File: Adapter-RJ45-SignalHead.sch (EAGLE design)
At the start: 4 parts, among them CON1 CONNECTOR-GROVE-4P-2.0-347013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, CON2 CONNECTOR-GROVE-4P-2.0-347013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

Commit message: V3.2 - added CUT-R
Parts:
- added CON3, CON4: (no value), SPCoast:CONNECTOR-M04LOCK
- added R1, R2, R3, R4, R5, R6: (no value), SPCoast:RPTH-R0
- CON1, CON2: value CONNECTOR-GROVE-4P-2.0-3470130P1 -> (none)
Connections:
- removed net L5: CON2.1, J1.5
- removed net L6: CON2.2, J1.6
- removed net L7: CON2.3, J1.7
- removed net L8: CON2.4, J1.8
- removed net N$1: CON1.1, J1.1
- removed net N$2: CON1.2, J1.2
- removed net N$3: CON1.3, J1.3
- removed net N$4: CON1.4, J1.4
- new net A-COMMON: CON1.4, CON4.4, J1.4
- new net AG: J1.1, R6.2
- new net AGR: CON1.1, CON4.1, R6.1
- new net AR: J1.3, R4.2
- new net ARR: CON1.3, CON4.3, R4.1
- new net AY: J1.2, R5.2
- new net AYR: CON1.2, CON4.2, R5.1
- new net B-COMMON: CON2.4, CON3.4, J1.8
- new net BG: J1.5, R3.2
- new net BGR: CON2.1, CON3.1, R3.1
- new net BR: J1.7, R1.2
- new net BRR: CON2.3, CON3.3, R1.1
- new net BY: J1.6, R2.2
- new net BYR: CON2.2, CON3.2, R2.1
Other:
- note added: "2x 2mm 4-pin"
- note added: "Signal Head Breakout"
- note added: "v3.2"
- note added: "w/ optional resistors"
- note removed: "CMRI Breakout"
- note removed: "RJ45 adapter"
- note removed: "v3.1"
- moved on the sheet: CON1, CON2, J1

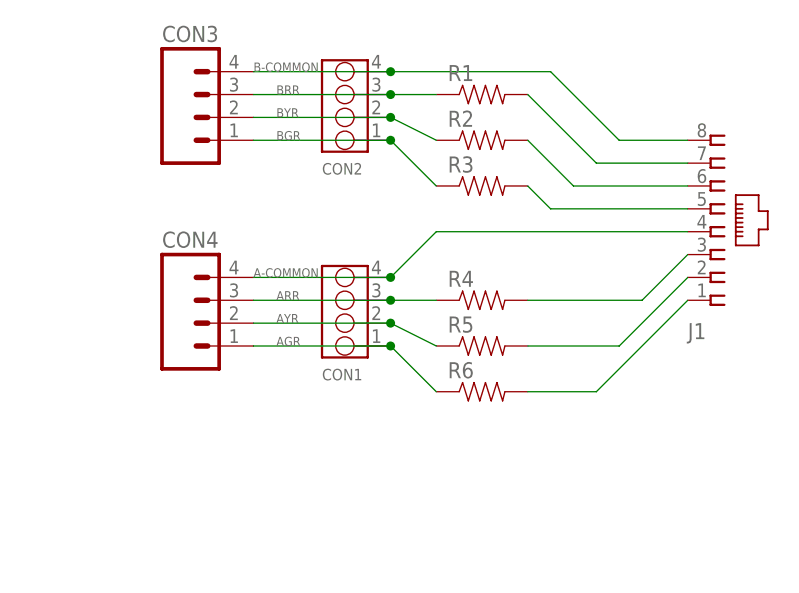
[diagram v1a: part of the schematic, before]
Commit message: added values for connectors
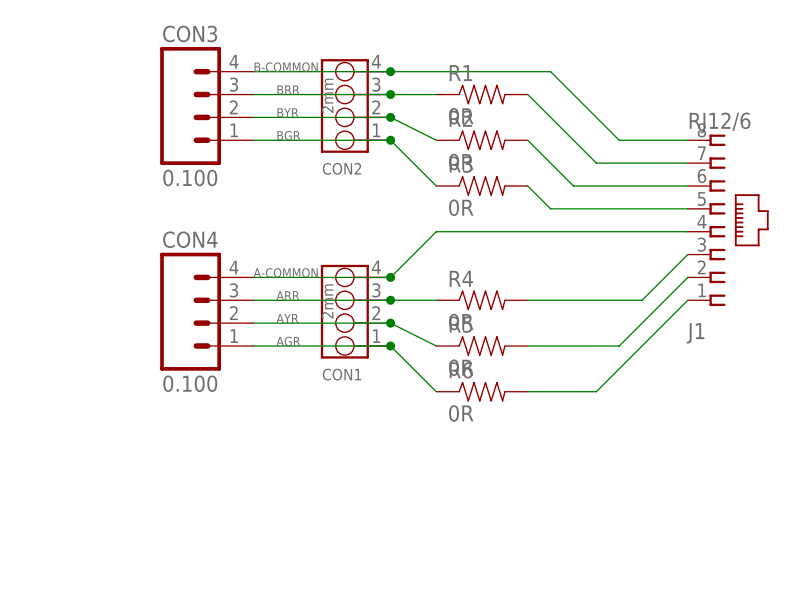
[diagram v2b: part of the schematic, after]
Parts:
- CON1, CON2: value (none) -> 2mm
- CON3, CON4: value (none) -> 0.100
- J1: value (none) -> RJ12/6
- R1, R2, R3, R4, R5, R6: value (none) -> 0R
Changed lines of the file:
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@@
 <grid distance="100" unitdist="mil" unit="mil" style="dots" multiple="1" display="yes" altdistance="50" altunitdist="mil" altunit="mil"/>
 <layers>
-<layer number="1" name="Top" color="4" fill="1" visible="yes" active="no"/>
-<layer number="2" name="Route2" color="1" fill="3" visible="yes" active="no"/>
-<layer number="3" name="Route3" color="4" fill="3" visible="yes" active="no"/>
-<layer number="14" name="Route14" color="1" fill="6" visible="yes" active="no"/>
-<layer number="15" name="Route15" color="4" fill="6" visible="yes" active="no"/>
-<layer number="16" name="Bottom" color="2" fill="1" visible="yes" active="no"/>
-<layer number="17" name="Pads" color="23" fill="1" visible="yes" active="no"/>
-<layer number="18" name="Vias" color="29" fill="1" visible="yes" active="no"/>
-<layer number="19" name="Unrouted" color="6" fill="1" visible="yes" active="no"/>
-<layer number="20" name="Dimension" color="15" fill="1" visible="yes" active="no"/>
-<layer number="21" name="tPlace" color="19" fill="1" visible="yes" active="no"/>
-<layer number="22" name="bPlace" color="17" fill="1" visible="yes" active="no"/>
-<layer number="23" name="tOrigins" color="30" fill="1" visible="yes" active="no"/>
-<layer number="24" name="bOrigins" color="15" fill="1" visible="yes" active="no"/>
-<layer number="25" name="tNames" color="63" fill="1" visible="yes" active="no"/>
-<layer number="26" name="bNames" color="34" fill="1" visible="yes" active="no"/>
-<layer number="27" name="tValues" color="56" fill="1" visible="yes" active="no"/>
-<layer number="28" name="bValues" color="7" fill="1" visible="yes" active="no"/>
+<layer number="1" name="Top" color="4" fill="1" visible="no" active="no"/>
+<layer number="2" name="Route2" color="1" fill="3" visible="no" active="no"/>
+<layer number="3" name="Route3" color="4" fill="3" visible="no" active="no"/>
+<layer number="14" name="Route14" color="1" fill="6" visible="no" active="no"/>
+<layer number="15" name="Route15" color="4" fill="6" visible="no" active="no"/>
+<layer number="16" name="Bottom" color="2" fill="1" visible="no" active="no"/>
+<layer number="17" name="Pads" color="23" fill="1" visible="no" active="no"/>
+<layer number="18" name="Vias" color="29" fill="1" visible="no" active="no"/>
+<layer number="19" name="Unrouted" color="6" fill="1" visible="no" active="no"/>
+<layer number="20" name="Dimension" color="15" fill="1" visible="no" active="no"/>
+<layer number="21" name="tPlace" color="19" fill="1" visible="no" active="no"/>
+<layer number="22" name="bPlace" color="17" fill="1" visible="no" active="no"/>
+<layer number="23" name="tOrigins" color="30" fill="1" visible="no" active="no"/>
+<layer number="24" name="bOrigins" color="15" fill="1" visible="no" active="no"/>
+<layer number="25" name="tNames" color="63" fill="1" visible="no" active="no"/>
+<layer number="26" name="bNames" color="34" fill="1" visible="no" active="no"/>
+<layer number="27" name="tValues" color="56" fill="1" visible="no" active="no"/>
+<layer number="28" name="bValues" color="7" fill="1" visible="no" active="no"/>
 <layer number="29" name="tStop" color="7" fill="3" visible="no" active="no"/>
 <layer number="30" name="bStop" color="7" fill="6" visible="no" active="no"/>
@@
 <layer number="35" name="tGlue" color="7" fill="4" visible="no" active="no"/>
 <layer number="36" name="bGlue" color="7" fill="5" visible="no" active="no"/>
-<layer number="37" name="tTest" color="7" fill="1" visible="yes" active="no"/>
-<layer number="38" name="bTest" color="7" fill="1" visible="yes" active="no"/>
+<layer number="37" name="tTest" color="7" fill="1" visible="no" active="no"/>
+<layer number="38" name="bTest" color="7" fill="1" visible="no" active="no"/>
 <layer number="39" name="tKeepout" color="4" fill="11" visible="no" active="no"/>
 <layer number="40" name="bKeepout" color="3" fill="11" visible="no" active="no"/>
@@
 <layer number="44" name="Drills" color="16" fill="1" visible="no" active="no"/>
 <layer number="45" name="Holes" color="35" fill="1" visible="no" active="no"/>
-<layer number="46" name="Milling" color="35" fill="1" visible="yes" active="no"/>
-<layer number="47" name="Measures" color="21" fill="1" visible="yes" active="no"/>
-<layer number="48" name="Document" color="36" fill="1" visible="yes" active="no"/>
-<layer number="49" name="Reference" color="48" fill="1" visible="yes" active="no"/>
-<layer number="50" name="dxf" color="7" fill="1" visible="yes" active="no"/>
-<layer number="51" name="tDocu" color="24" fill="1" visible="yes" active="no"/>
-<layer number="52" name="bDocu" color="7" fill="1" visible="yes" active="no"/>
-<layer number="53" name="tGND_GNDA" color="7" fill="9" visible="yes" active="no"/>
-<layer number="54" name="bGND_GNDA" color="1" fill="9" visible="yes" active="no"/>
-<layer number="56" name="wert" color="7" fill="1" visible="yes" active="no"/>
-<layer number="57" name="tCAD" color="7" fill="1" visible="yes" active="no"/>
-<layer number="59" name="tCarbon" color="7" fill="1" visible="yes" active="no"/>
-<layer number="60" name="bCarbon" color="7" fill="1" visible="yes" active="no"/>
+<layer number="46" name="Milling" color="35" fill="1" visible="no" active="no"/>
+<layer number="47" name="Measures" color="21" fill="1" visible="no" active="no"/>
+<layer number="48" name="Document" color="36" fill="1" visible="no" active="no"/>
+<layer number="49" name="Reference" color="48" fill="1" visible="no" active="no"/>
+<layer number="50" name="dxf" color="7" fill="1" visible="no" active="no"/>
+<layer number="51" name="tDocu" color="24" fill="1" visible="no" active="no"/>
+<layer number="52" name="bDocu" color="7" fill="1" visible="no" active="no"/>
+<layer number="53" name="tGND_GNDA" color="7" fill="9" visible="no" active="no"/>
+<layer number="54" name="bGND_GNDA" color="1" fill="9" visible="no" active="no"/>
+<layer number="56" name="wert" color="7" fill="1" visible="no" active="no"/>
+<layer number="57" name="tCAD" color="7" fill="1" visible="no" active="no"/>
+<layer number="59" name="tCarbon" color="7" fill="1" visible="no" active="no"/>
+<layer number="60" name="bCarbon" color="7" fill="1" visible="no" active="no"/>
 <layer number="90" name="Modules" color="5" fill="1" visible="yes" active="yes"/>
 <layer number="91" name="Nets" color="2" fill="1" visible="yes" active="yes"/>
@@
 <part name="FRAME1" library="SparkFun" deviceset="FRAME-LETTER" device=""/>
 <part name="U$1" library="SPCoast" deviceset="DOC-OSHW-LOGO-" device="M"/>
-<part name="CON1" library="SPCoast" deviceset="CONNECTOR-GROVE-4P-2.0" device="-3470130P1"/>
-<part name="CON2" library="SPCoast" deviceset="CONNECTOR-GROVE-4P-2.0" device="-3470130P1"/>
-<part name="R1" library="SPCoast" deviceset="R*" device="PTH-R0"/>
-<part name="R2" library="SPCoast" deviceset="R*" device="PTH-R0"/>
-<part name="R3" library="SPCoast" deviceset="R*" device="PTH-R0"/>
-<part name="R4" library="SPCoast" deviceset="R*" device="PTH-R0"/>
-<part name="R5" library="SPCoast" deviceset="R*" device="PTH-R0"/>
-<part name="R6" library="SPCoast" deviceset="R*" device="PTH-R0"/>
-<part name="J1" library="SPCoast" deviceset="CONNECTOR-RJ45" device="-FRONT"/>
-<part name="CON3" library="SPCoast" deviceset="CONNECTOR-M04" device="LOCK"/>
-<part name="CON4" library="SPCoast" deviceset="CONNECTOR-M04" device="LOCK"/>
+<part name="CON1" library="SPCoast" deviceset="CONNECTOR-GROVE-4P-2.0" device="-3470130P1" value="2mm"/>
+<part name="CON2" library="SPCoast" deviceset="CONNECTOR-GROVE-4P-2.0" device="-3470130P1" value="2mm"/>
+<part name="R1" library="SPCoast" deviceset="R*" device="PTH-R0" value="0R"/>
+<part name="R2" library="SPCoast" deviceset="R*" device="PTH-R0" value="0R"/>
+<part name="R3" library="SPCoast" deviceset="R*" device="PTH-R0" value="0R"/>
+<part name="R4" library="SPCoast" deviceset="R*" device="PTH-R0" value="0R"/>
+<part name="R5" library="SPCoast" deviceset="R*" device="PTH-R0" value="0R"/>
+<part name="R6" library="SPCoast" deviceset="R*" device="PTH-R0" value="0R"/>
+<part name="J1" library="SPCoast" deviceset="CONNECTOR-RJ45" device="-FRONT" value="RJ12/6"/>
+<part name="CON3" library="SPCoast" deviceset="CONNECTOR-M04" device="LOCK" value="0.100"/>
+<part name="CON4" library="SPCoast" deviceset="CONNECTOR-M04" device="LOCK" value="0.100"/>
 </parts>
 <sheets>

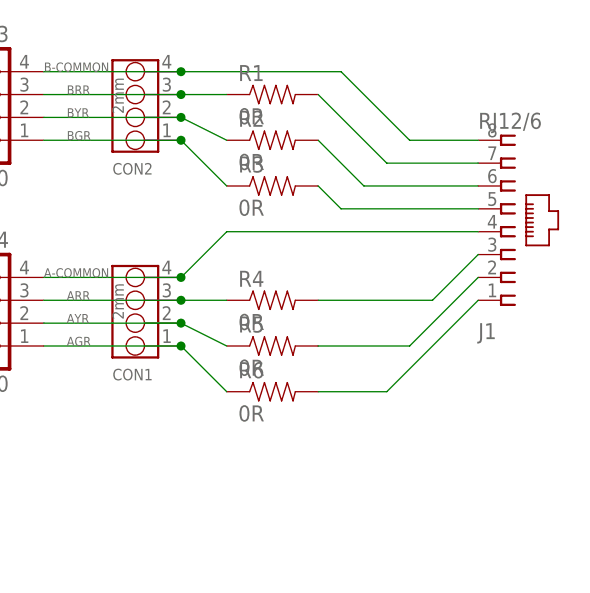
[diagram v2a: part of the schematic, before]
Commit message: normalized values
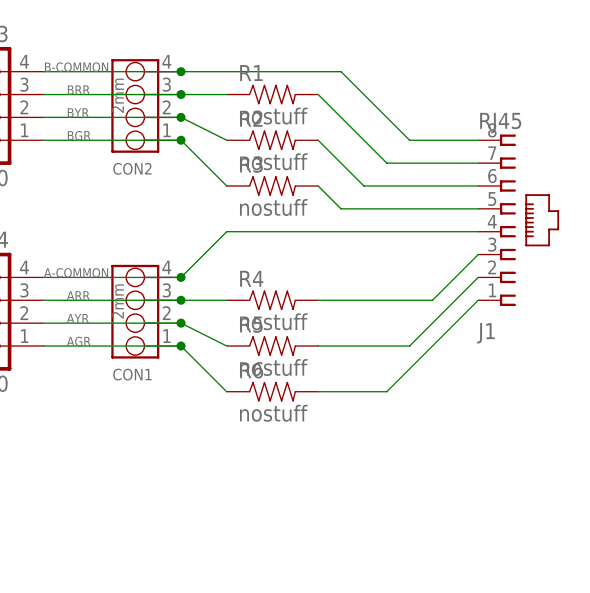
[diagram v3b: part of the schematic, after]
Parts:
- J1: value RJ12/6 -> RJ45
- R1, R2, R3, R4, R5, R6: value 0R -> nostuff
- U$1: value DOC-OSHW-LOGO-M -> OSHW
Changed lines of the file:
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@@
 <parts>
 <part name="FRAME1" library="SparkFun" deviceset="FRAME-LETTER" device=""/>
-<part name="U$1" library="SPCoast" deviceset="DOC-OSHW-LOGO-" device="M"/>
+<part name="U$1" library="SPCoast" deviceset="DOC-OSHW-LOGO-" device="M" value="OSHW"/>
 <part name="CON1" library="SPCoast" deviceset="CONNECTOR-GROVE-4P-2.0" device="-3470130P1" value="2mm"/>
 <part name="CON2" library="SPCoast" deviceset="CONNECTOR-GROVE-4P-2.0" device="-3470130P1" value="2mm"/>
-<part name="R1" library="SPCoast" deviceset="R*" device="PTH-R0" value="0R"/>
-<part name="R2" library="SPCoast" deviceset="R*" device="PTH-R0" value="0R"/>
-<part name="R3" library="SPCoast" deviceset="R*" device="PTH-R0" value="0R"/>
-<part name="R4" library="SPCoast" deviceset="R*" device="PTH-R0" value="0R"/>
-<part name="R5" library="SPCoast" deviceset="R*" device="PTH-R0" value="0R"/>
-<part name="R6" library="SPCoast" deviceset="R*" device="PTH-R0" value="0R"/>
-<part name="J1" library="SPCoast" deviceset="CONNECTOR-RJ45" device="-FRONT" value="RJ12/6"/>
+<part name="R1" library="SPCoast" deviceset="R*" device="PTH-R0" value="nostuff"/>
+<part name="R2" library="SPCoast" deviceset="R*" device="PTH-R0" value="nostuff"/>
+<part name="R3" library="SPCoast" deviceset="R*" device="PTH-R0" value="nostuff"/>
+<part name="R4" library="SPCoast" deviceset="R*" device="PTH-R0" value="nostuff"/>
+<part name="R5" library="SPCoast" deviceset="R*" device="PTH-R0" value="nostuff"/>
+<part name="R6" library="SPCoast" deviceset="R*" device="PTH-R0" value="nostuff"/>
+<part name="J1" library="SPCoast" deviceset="CONNECTOR-RJ45" device="-FRONT" value="RJ45"/>
 <part name="CON3" library="SPCoast" deviceset="CONNECTOR-M04" device="LOCK" value="0.100"/>
 <part name="CON4" library="SPCoast" deviceset="CONNECTOR-M04" device="LOCK" value="0.100"/>
